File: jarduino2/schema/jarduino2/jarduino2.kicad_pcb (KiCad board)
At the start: 2 copper layers, 93 x 89 mm, 52 parts, among them J1 Alimentations 12V, J2 Cmd Mcu, J3 Commandes, J4 Pompe1, J5 Pompe 2, J6 Ext, J8 Program, J9 Tests, Q1 Q_NPN_BCE, Q2 Q_NPN_BCE, SW1 SW_Push, U1 R-78B3.3-2.0, U2 MSP430F1222IDW, U3 RtcArduino

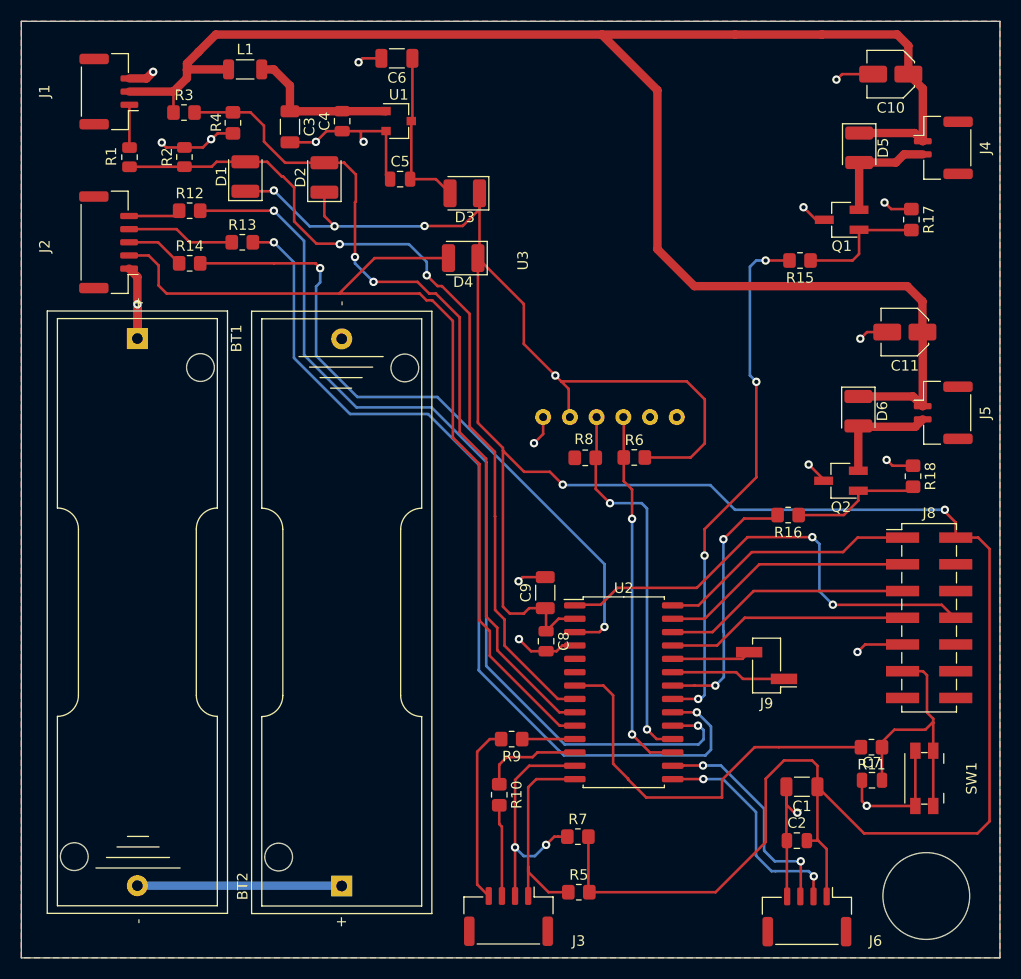
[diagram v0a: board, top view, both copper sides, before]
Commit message: Amélioration proto: - Diametre trous de fixation 4mm (avec compo sepcial) - SW1/SW2 echanges Batt/Sol
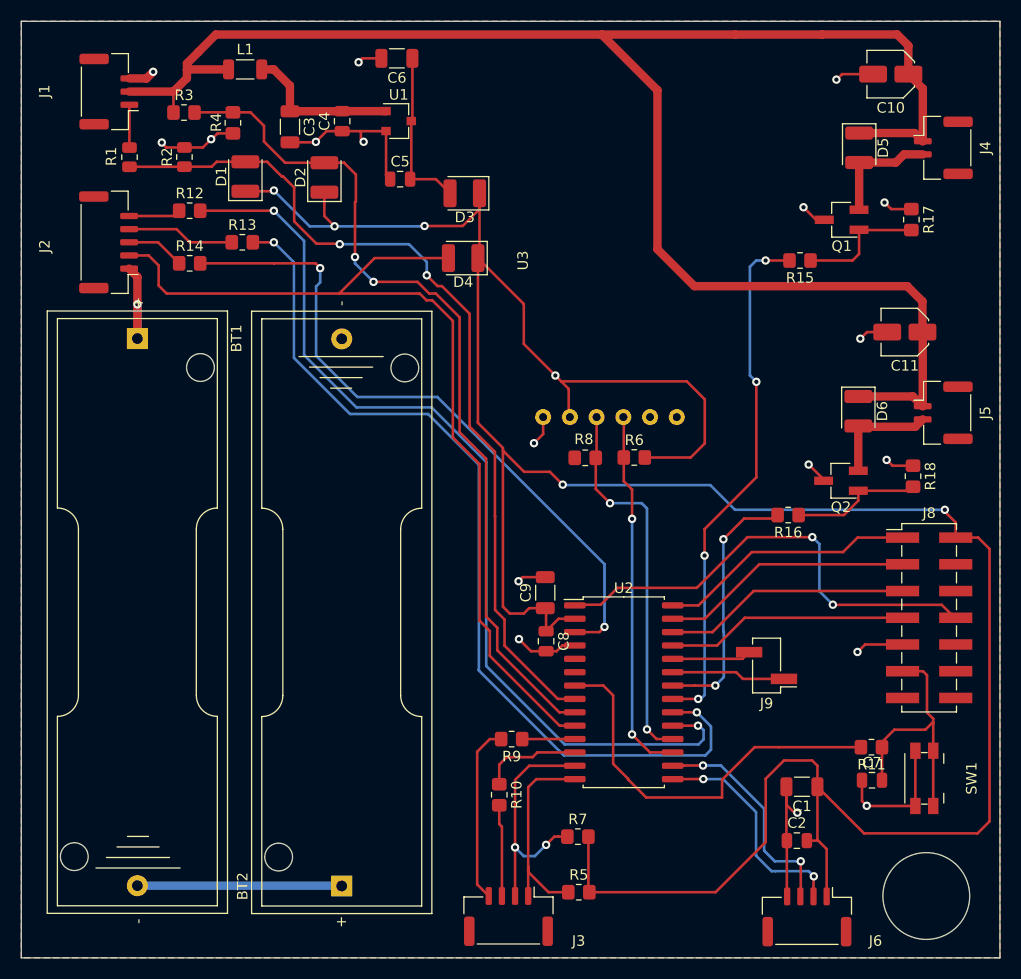
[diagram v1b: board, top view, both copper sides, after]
